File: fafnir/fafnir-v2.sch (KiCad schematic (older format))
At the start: 16 parts, among them IC1 CD4049UBE

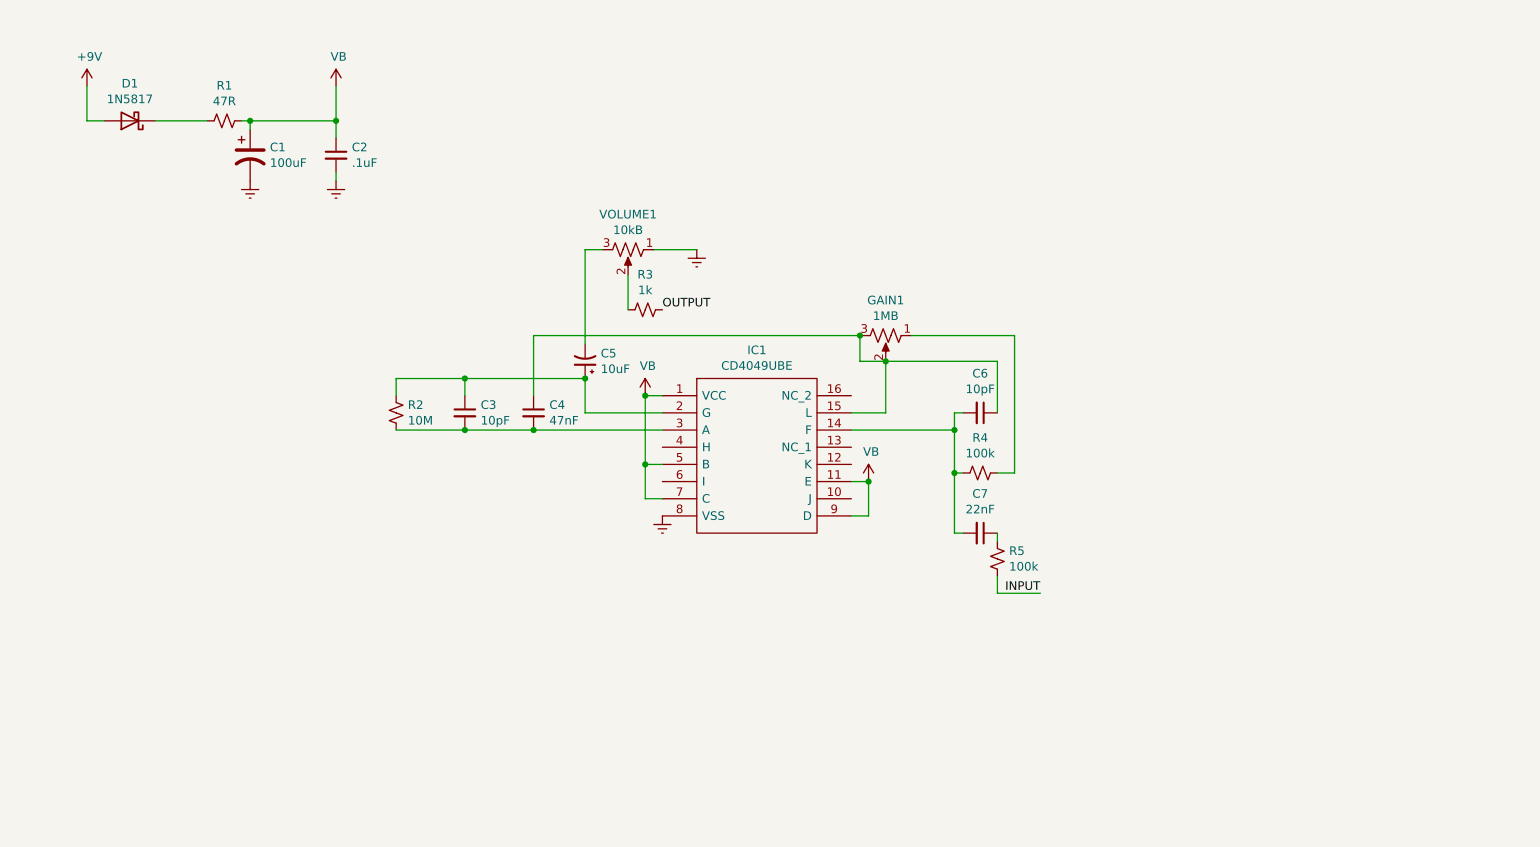
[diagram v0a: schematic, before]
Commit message: using CD4049UBE for bax
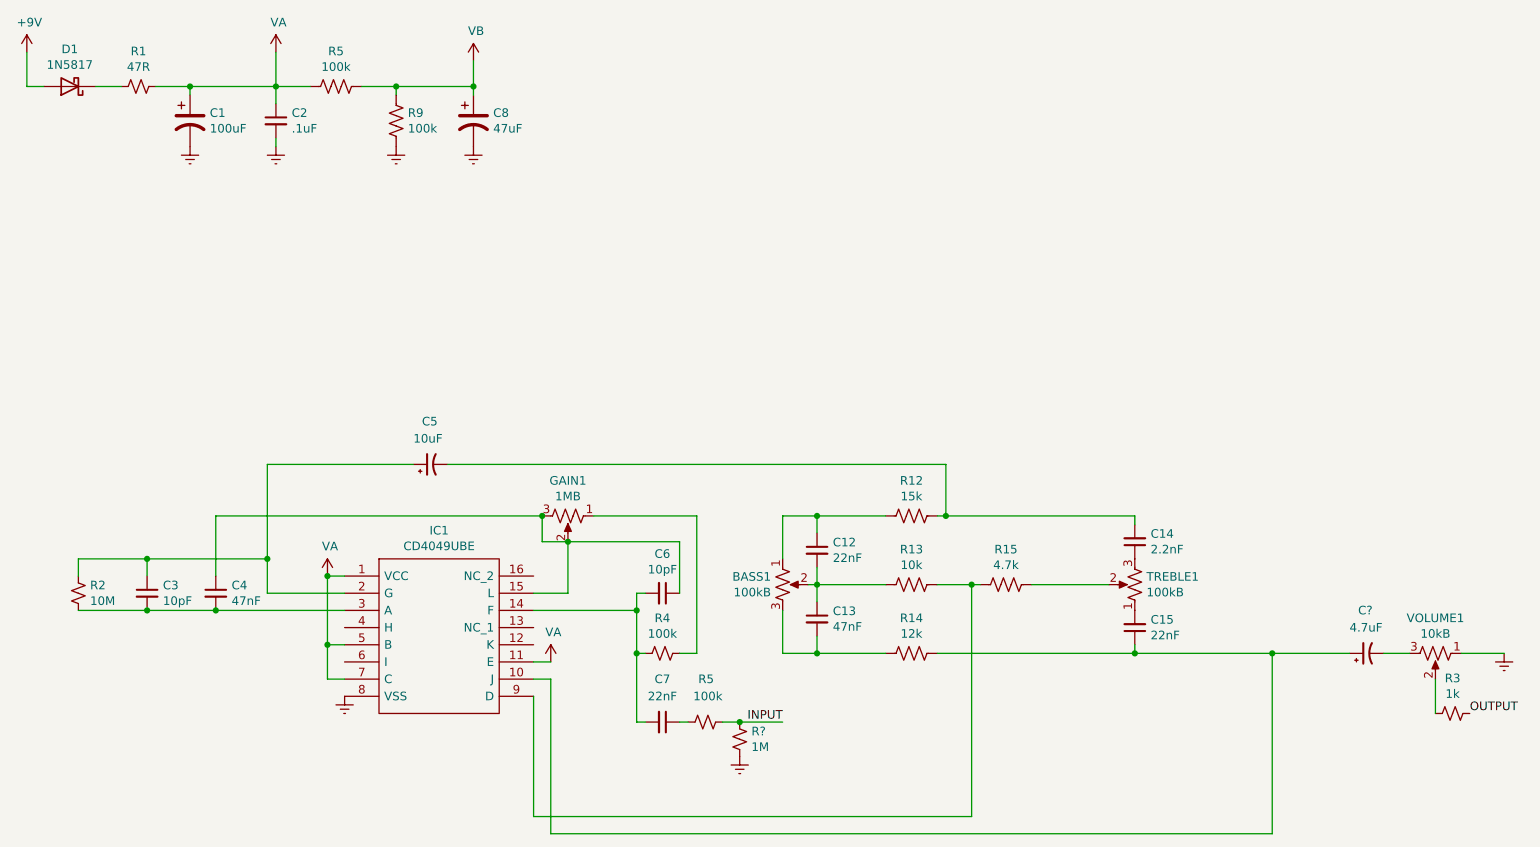
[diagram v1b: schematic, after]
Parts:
- added BASS1, TREBLE1: 100kB, potentiometers:16MM_T.MOUNT, symbol Device:R_POT_US
- added C12, C15: 22nF, caps-film:0.2_.SML, symbol Device:C_Small
- added C13: 47nF, caps-film:0.2_.SML, symbol Device:C_Small
- added C14: 2.2nF, caps-film:0.2_.SML, symbol Device:C_Small
- added C8: 47uF, caps-elec:050.FLAT, symbol Device:CP1
- added C?: 4.7uF, symbol Device:CP1_Small
- added R12: 15k, resistors:0.2_, symbol Device:R_US
- added R13: 10k, resistors:0.2_, symbol Device:R_US
- added R14: 12k, resistors:0.2_, symbol Device:R_US
- added R15: 4.7k, resistors:0.2_, symbol Device:R_US
- added R5, R9: 100k, resistors:0.2_, symbol Device:R_US
- added R?: 1M, symbol Device:R_Small_US
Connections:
- net Earth: now also C8.2, R9.2, R?.2
- net INPUT: now also R?.1
- net VAB: now also C8.1, R5.1, R9.1; no longer C1.1, C2.1, IC1.1 (VCC), IC1.11 (E), IC1.5 (B), IC1.7 (C), IC1.9 (D), R1.1
- net at IC1.10 (J): now also C15.1, C?.1, R14.1
- net at C5.2: now also C14.2, R12.1; no longer VOLUME1.3
- new net: BASS1.1, C12.1, R12.2
- new net: BASS1.2, C12.2, C13.1, R13.2
- new net: BASS1.3, C13.2, R14.2
- new net: IC1.9 (D), R13.1, R15.2
- new net: R15.1, TREBLE1.2
- new net: C15.2, TREBLE1.1
- new net: C14.1, TREBLE1.3
- new net: C?.2, VOLUME1.3
- new net VAA: C1.1, C2.1, IC1.1 (VCC), IC1.11 (E), IC1.5 (B), IC1.7 (C), R1.1, R5.2
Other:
- moved on the sheet: C1, C2, C3, C4, C5, C6, C7, D1, GAIN1, IC1, R1, R2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

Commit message: moved volume before bax, seems to work better
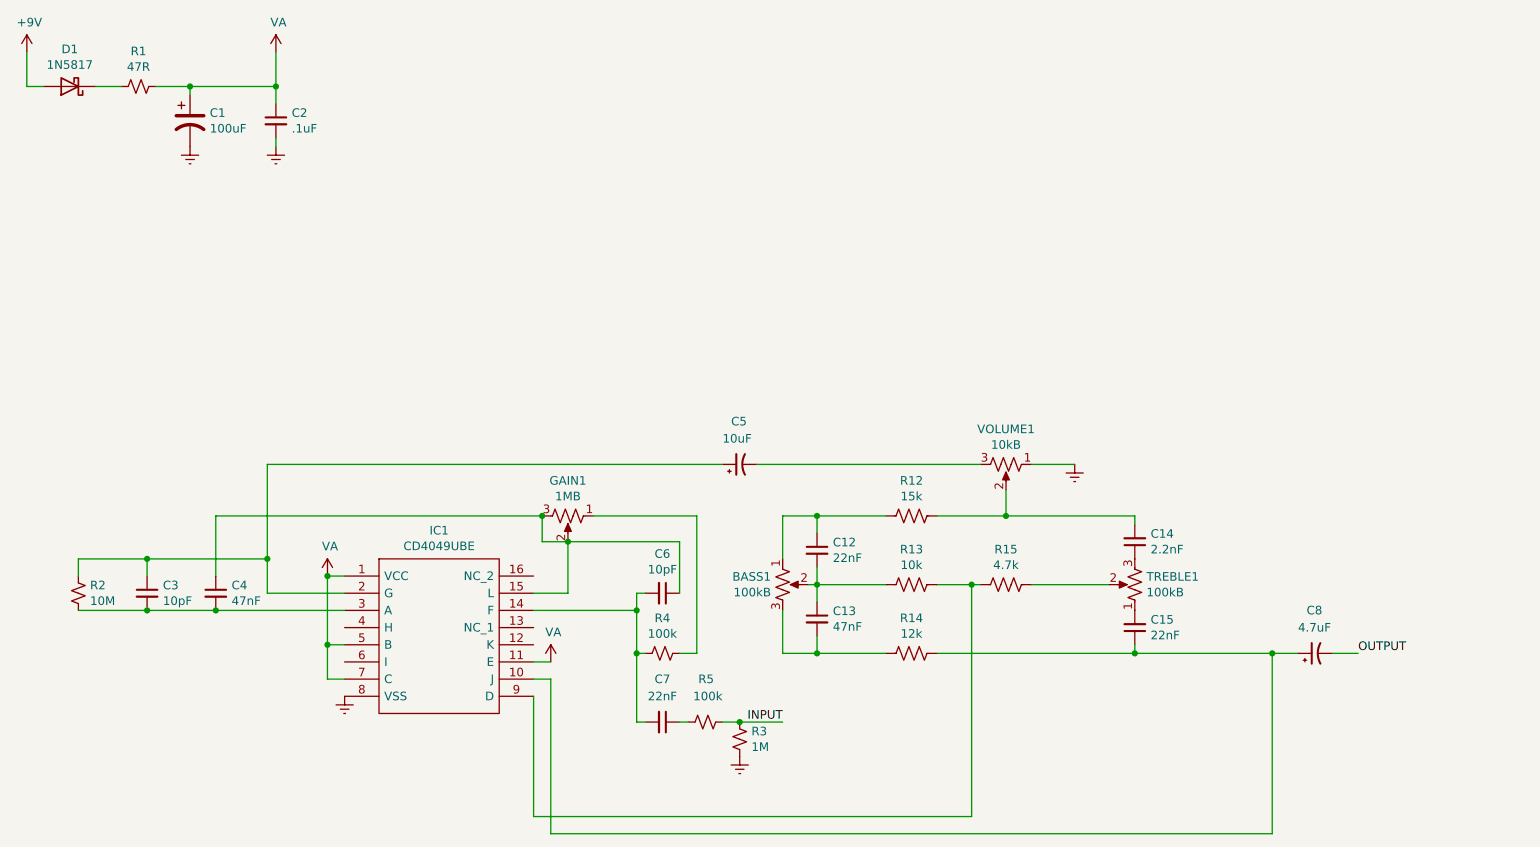
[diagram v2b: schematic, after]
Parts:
- removed C8: 47uF, caps-elec:050.FLAT, symbol Device:CP1
- removed R3: 1k, symbol Device:R_Small_US
- removed R5, R9: 100k, resistors:0.2_, symbol Device:R_US
- gave numbers to parts that had none: 2
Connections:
- net OUTPUT: now also C8.2
- net at C14.2, R12.1: now also VOLUME1.2; no longer C5.2
- net at VOLUME1.3: now also C5.2; no longer C8.2
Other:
- moved on the sheet: C5, C8, VOLUME1
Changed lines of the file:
@@
 	2600 4450 4500 4450
 Connection ~ 4500 4450
-$Comp
-L Device:R_Small_US R3
-U 1 1 5F9EAB3B
-P 9800 5600
-F 0 "R3" V 9595 5600 50  0000 C CNN
-F 1 "1k" V 9686 5600 50  0000 C CNN
-F 2 "" H 9800 5600 50  0001 C CNN
-F 3 "~" H 9800 5600 50  0001 C CNN
-	1    9800 5600
-	0    1    1    0
-$EndComp
-Text Label 9900 5600 0    50   ~ 0
-OUTPUT
 Wire Wire Line
 	1800 4800 1800 4700
@@
 $EndComp
 Wire Wire Line
-	6800 4450 6850 4450
-Wire Wire Line
 	6800 4850 7000 4850
 Connection ~ 7000 4850
 Wire Wire Line
 	7000 4850 7050 4850
-Wire Wire Line
-	6850 4150 6850 4450
-Connection ~ 6850 4450
-Wire Wire Line
-	6850 4450 7950 4450
 Wire Wire Line
 	6800 5250 7950 5250
@@
 	7350 4850 7800 4850
 Connection ~ 7950 5250
-Connection ~ 4100 1950
-Wire Wire Line
-	4100 1800 4100 1950
-$Comp
-L power:VB #PWR015
-U 1 1 5F1E202E
-P 4100 1800
-F 0 "#PWR015" H 4100 1650 50  0001 C CNN
-F 1 "VB" H 4115 1973 50  0000 C CNN
-F 2 "" H 4100 1800 50  0001 C CNN
-F 3 "" H 4100 1800 50  0001 C CNN
-	1    4100 1800
-	1    0    0    -1
-$EndComp
-Connection ~ 3650 1950
-Wire Wire Line
-	4100 1950 4100 2000
-Wire Wire Line
-	3650 1950 4100 1950
-$Comp
-L Device:CP1 C8
-U 1 1 5F1DE6F4
-P 4100 2150
-F 0 "C8" H 4215 2196 50  0000 L CNN
-F 1 "47uF" H 4215 2105 50  0000 L CNN
-F 2 "caps-elec:050.FLAT" H 4100 2150 50  0001 C CNN
-F 3 "~" H 4100 2150 50  0001 C CNN
-	1    4100 2150
-	1    0    0    -1
-$EndComp
-Wire Wire Line
-	3650 1950 3650 2000
-Wire Wire Line
-	3450 1950 3650 1950
-$Comp
-L Device:R_US R9
-U 1 1 5F1DC0E7
-P 3650 2150
-F 0 "R9" H 3718 2196 50  0000 L CNN
-F 1 "100k" H 3718 2105 50  0000 L CNN
-F 2 "resistors:0.2_" V 3690 2140 50  0001 C CNN
-F 3 "~" H 3650 2150 50  0001 C CNN
-	1    3650 2150
-	1    0    0    -1
-$EndComp
-$Comp
-L Device:R_US R5
-U 1 1 5F1DA6DA
-P 3300 1950
-F 0 "R5" V 3095 1950 50  0000 C CNN
-F 1 "100k" V 3186 1950 50  0000 C CNN
-F 2 "resistors:0.2_" V 3340 1940 50  0001 C CNN
-F 3 "~" H 3300 1950 50  0001 C CNN
-	1    3300 1950
-	0    1    1    0
-$EndComp
 $Comp
 L Device:R_POT_US TREBLE1
@@
 $EndComp
 $Comp
-L power:VA #PWR?
+L power:VA #PWR03
 U 1 1 5FB79811
 P 2950 1750
-F 0 "#PWR?" H 2950 1600 50  0001 C CNN
+F 0 "#PWR03" H 2950 1600 50  0001 C CNN
 F 1 "VA" H 2965 1923 50  0000 C CNN
 F 2 "" H 2950 1750 50  0001 C CNN
@@
 $EndComp
 $Comp
-L power:VA #PWR?
+L power:VA #PWR05
 U 1 1 5FB7E32C
 P 3250 4800
-F 0 "#PWR?" H 3250 4650 50  0001 C CNN
+F 0 "#PWR05" H 3250 4650 50  0001 C CNN
 F 1 "VA" H 3265 4973 50  0000 C CNN
 F 2 "" H 3250 4800 50  0001 C CNN
@@
 Connection ~ 3250 4800
 $Comp
-L power:VA #PWR?
+L power:VA #PWR08
 U 1 1 5FB7E813
 P 4550 5300
-F 0 "#PWR?" H 4550 5150 50  0001 C CNN
+F 0 "#PWR08" H 4550 5150 50  0001 C CNN
 F 1 "VA" H 4565 5473 50  0000 C CNN
 F 2 "" H 4550 5300 50  0001 C CNN
@@
 	1    0    0    -1
 $EndComp
-Wire Wire Line
-	2950 1950 3150 1950
-$Comp
-L power:Earth #PWR?
-U 1 1 5FB8F356
-P 3650 2300
-F 0 "#PWR?" H 3650 2050 50  0001 C CNN
-F 1 "Earth" H 3650 2150 50  0001 C CNN
-F 2 "" H 3650 2300 50  0001 C CNN
-F 3 "~" H 3650 2300 50  0001 C CNN
-	1    3650 2300
-	1    0    0    -1
-$EndComp
-$Comp
-L power:Earth #PWR?
-U 1 1 5FB8F35C
-P 4100 2300
-F 0 "#PWR?" H 4100 2050 50  0001 C CNN
-F 1 "Earth" H 4100 2150 50  0001 C CNN
-F 2 "" H 4100 2300 50  0001 C CNN
-F 3 "~" H 4100 2300 50  0001 C CNN
-	1    4100 2300
-	1    0    0    -1
-$EndComp
-Wire Wire Line
-	9850 5250 10100 5250
-$Comp
-L power:Earth #PWR07
-U 1 1 5F9E9D23
-P 10100 5250
-F 0 "#PWR07" H 10100 5000 50  0001 C CNN
-F 1 "Earth" H 10100 5100 50  0001 C CNN
-F 2 "" H 10100 5250 50  0001 C CNN
-F 3 "~" H 10100 5250 50  0001 C CNN
-	1    10100 5250
-	1    0    0    -1
-$EndComp
-Wire Wire Line
-	9700 5400 9700 5600
-$Comp
-L Device:R_POT_US VOLUME1
-U 1 1 5F9E6D42
-P 9700 5250
-F 0 "VOLUME1" V 9495 5250 50  0000 C CNN
-F 1 "10kB" V 9586 5250 50  0000 C CNN
-F 2 "" H 9700 5250 50  0001 C CNN
-F 3 "~" H 9700 5250 50  0001 C CNN
-	1    9700 5250
-	0    1    1    0
-$EndComp
-$Comp
-L Device:CP1_Small C5
-U 1 1 5F9D30EF
-P 3850 4150
-F 0 "C5" V 4100 4200 50  0000 R CNN
-F 1 "10uF" V 4000 4250 50  0000 R CNN
-F 2 "" H 3850 4150 50  0001 C CNN
-F 3 "~" H 3850 4150 50  0001 C CNN
-	1    3850 4150
-	0    -1   -1   0
-$EndComp
 Connection ~ 2900 4700
 Wire Wire Line
-	2900 4150 3750 4150
-Wire Wire Line
 	2900 4150 2900 4700
-Wire Wire Line
-	3950 4150 6850 4150
-$Comp
-L Device:CP1_Small C?
+$Comp
+L Device:CP1_Small C8
 U 1 1 5FBE3354
-P 9300 5250
-F 0 "C?" V 9550 5300 50  0000 R CNN
-F 1 "4.7uF" V 9450 5350 50  0000 R CNN
-F 2 "" H 9300 5250 50  0001 C CNN
-F 3 "~" H 9300 5250 50  0001 C CNN
-	1    9300 5250
+P 9000 5250
+F 0 "C8" V 9250 5300 50  0000 R CNN
+F 1 "4.7uF" V 9150 5350 50  0000 R CNN
+F 2 "" H 9000 5250 50  0001 C CNN
+F 3 "~" H 9000 5250 50  0001 C CNN
+	1    9000 5250
 	0    -1   -1   0
 $EndComp
@@
 	1900 1950 2050 1950
 Wire Wire Line
-	9400 5250 9550 5250
-Wire Wire Line
 	7000 6200 4450 6200
 Wire Wire Line
@@
 Wire Wire Line
 	4550 5400 4450 5400
-Connection ~ 8750 5250
-Wire Wire Line
-	8750 5250 9200 5250
 Wire Wire Line
 	5050 5250 5050 5650
@@
 	5050 5650 5100 5650
 $Comp
-L Device:R_Small_US R?
+L Device:R_Small_US R3
 U 1 1 603C2E7B
 P 5650 5750
-F 0 "R?" H 5718 5796 50  0000 L CNN
+F 0 "R3" H 5718 5796 50  0000 L CNN
 F 1 "1M" H 5718 5705 50  0000 L CNN
 F 2 "" H 5650 5750 50  0001 C CNN
@@
 $EndComp
 $Comp
-L power:Earth #PWR?
+L power:Earth #PWR09
 U 1 1 603C3E4C
 P 5650 5850
-F 0 "#PWR?" H 5650 5600 50  0001 C CNN
+F 0 "#PWR09" H 5650 5600 50  0001 C CNN
 F 1 "Earth" H 5650 5700 50  0001 C CNN
 F 2 "" H 5650 5850 50  0001 C CNN
@@
 $EndComp
 Connection ~ 5650 5650
+Wire Wire Line
+	6800 4450 7200 4450
+$Comp
+L Device:R_POT_US VOLUME1
+U 1 1 5F9E6D42
+P 7200 4150
+F 0 "VOLUME1" V 6995 4150 50  0000 C CNN
+F 1 "10kB" V 7086 4150 50  0000 C CNN
+F 2 "" H 7200 4150 50  0001 C CNN
+F 3 "~" H 7200 4150 50  0001 C CNN
+	1    7200 4150
+	0    1    1    0
+$EndComp
+$Comp
+L power:Earth #PWR07
+U 1 1 5F9E9D23
+P 7600 4150
+F 0 "#PWR07" H 7600 3900 50  0001 C CNN
+F 1 "Earth" H 7600 4000 50  0001 C CNN
+F 2 "" H 7600 4150 50  0001 C CNN
+F 3 "~" H 7600 4150 50  0001 C CNN
+	1    7600 4150
+	1    0    0    -1
+$EndComp
+Wire Wire Line
+	7350 4150 7600 4150
+Wire Wire Line
+	7200 4300 7200 4450
+Connection ~ 7200 4450
+Wire Wire Line
+	7200 4450 7950 4450
+$Comp
+L Device:CP1_Small C5
+U 1 1 5F9D30EF
+P 5650 4150
+F 0 "C5" V 5900 4200 50  0000 R CNN
+F 1 "10uF" V 5800 4250 50  0000 R CNN
+F 2 "" H 5650 4150 50  0001 C CNN
+F 3 "~" H 5650 4150 50  0001 C CNN
+	1    5650 4150
+	0    -1   -1   0
+$EndComp
+Wire Wire Line
+	2900 4150 5550 4150
+Wire Wire Line
+	5750 4150 7050 4150
+Text Label 9250 5250 0    50   ~ 0
+OUTPUT
+Wire Wire Line
+	8750 5250 8900 5250
+Connection ~ 8750 5250
+Wire Wire Line
+	9100 5250 9250 5250
 $EndSCHEMATC
